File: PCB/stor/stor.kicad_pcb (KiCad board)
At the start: 2 copper layers, 21 x 55 mm, 45 parts, among them J1 Conn_01x04_Socket, SW1 TS1603-TZ38HBM, SW2 TS1603-TZ38HBM, U1 STM32H723VGT6, U2 TYPE-C 24P-GTJB 040, U3 USB3300-EZK-TR, U4 TPS62177DQCR, X1 25mhz, X2 32.768k, X3 24mhz

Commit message: all placed
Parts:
- moved C7 66.0 mm to (113.3, 50.0)
- moved C26 62.2 mm to (115.8, 68.7), turned to 90 degrees
- moved C17 60.5 mm to (121.3, 48.2)
- moved C10 56.8 mm to (114.5, 68.6), turned to 90 degrees
- moved C8 55.3 mm to (113.6, 64.8)
- moved C3 53.8 mm to (115.1, 66.8)
- moved C6 52.6 mm to (128.8, 50.1), turned to -90 degrees
- moved C4 48.1 mm to (121.0, 68.9), turned to 90 degrees
- moved C9 43.7 mm to (128.2, 65.3), turned to 90 degrees
- moved C5 42.2 mm to (129.5, 65.2), turned to 90 degrees
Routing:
- added copper zone on F.Cu, net GND

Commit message: pours
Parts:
- moved R4 2.70 mm to (129.1, 43.2)
- moved C16 2.41 mm to (126.7, 44.8)
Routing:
- added copper zone on In2.Cu, net /VDD
- added copper zone on B.Cu, net GND
- added copper zone on In1.Cu, net GND
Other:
- board size 21 x 55 mm -> 21 x 55.7 mm
- copper layers 2 -> 4
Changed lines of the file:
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@@
 	(layers
 		(0 "F.Cu" signal)
+		(4 "In1.Cu" signal)
+		(6 "In2.Cu" signal)
 		(2 "B.Cu" signal)
 		(9 "F.Adhes" user "F.Adhesive")
@@
 	)
 	(setup
+		(stackup
+			(layer "F.SilkS"
+				(type "Top Silk Screen")
+			)
+			(layer "F.Paste"
+				(type "Top Solder Paste")
+			)
+			(layer "F.Mask"
+				(type "Top Solder Mask")
+				(thickness 0.01)
+			)
+			(layer "F.Cu"
+				(type "copper")
+				(thickness 0.035)
+			)
+			(layer "dielectric 1"
+				(type "prepreg")
+				(thickness 0.1)
+				(material "FR4")
+				(epsilon_r 4.5)
+				(loss_tangent 0.02)
+			)
+			(layer "In1.Cu"
+				(type "copper")
+				(thickness 0.035)
+			)
+			(layer "dielectric 2"
+				(type "core")
+				(thickness 1.24)
+				(material "FR4")
+				(epsilon_r 4.5)
+				(loss_tangent 0.02)
+			)
+			(layer "In2.Cu"
+				(type "copper")
+				(thickness 0.035)
+			)
+			(layer "dielectric 3"
+				(type "prepreg")
+				(thickness 0.1)
+				(material "FR4")
+				(epsilon_r 4.5)
+				(loss_tangent 0.02)
+			)
+			(layer "B.Cu"
+				(type "copper")
+				(thickness 0.035)
+			)
+			(layer "B.Mask"
+				(type "Bottom Solder Mask")
+				(thickness 0.01)
+			)
+			(layer "B.Paste"
+				(type "Bottom Solder Paste")
+			)
+			(layer "B.SilkS"
+				(type "Bottom Silk Screen")
+			)
+			(copper_finish "None")
+			(dielectric_constraints no)
+		)
 		(pad_to_mask_clearance 0)
 		(allow_soldermask_bridges_in_footprints no)
@@
 		(capping no)
 		(filling no)
+		(zone_defaults)
 		(pcbplotparams
 			(layerselection 0x00000000_00000000_55555555_5755f5ff)
@@
 	(footprint "easyeda2kicad:R0402"
 		(layer "F.Cu")
-		(at 126.82 44.75)
+		(at 129.07 43.25)
 		(descr "200KΩ (2003) ±1%")
 		(property "Reference" "R4"
@@
 				(font
 					(size 1.27 1.27)
+					(thickness 0.15)
 				)
 			)
@@
 				(font
 					(size 1.27 1.27)
+					(thickness 0.15)
 				)
 			)
@@
 				(font
 					(size 1.27 1.27)
+					(thickness 0.15)
 				)
 			)
@@
 				(font
 					(size 1.27 1.27)
+					(thickness 0.15)
 				)
 			)
@@
 				(font
 					(size 1.27 1.27)
+					(thickness 0.15)
 				)
 			)
@@
 				(font
 					(size 1.27 1.27)
+					(thickness 0.15)
 				)
 			)
@@
 				(font
 					(size 1.27 1.27)
+					(thickness 0.15)
 				)
 			)
@@
 				(font
 					(size 1.27 1.27)
+					(thickness 0.15)
 				)
 			)
@@
 				(font
 					(size 1.27 1.27)
+					(thickness 0.15)
 				)
 			)
@@
 				(font
 					(size 1.27 1.27)
+					(thickness 0.15)
 				)
 			)
@@
 				(font
 					(size 1.27 1.27)
+					(thickness 0.15)
 				)
 			)
@@
 				(font
 					(size 1.27 1.27)
+					(thickness 0.15)
 				)
 			)
@@
 				(font
 					(size 1.27 1.27)
+					(thickness 0.15)
 				)
 			)
@@
 				(font
 					(size 1.27 1.27)
+					(thickness 0.15)
 				)
 			)
@@
 				(font
 					(size 1.27 1.27)
+					(thickness 0.15)
 				)
 			)
@@
 				(font
 					(size 1.27 1.27)
+					(thickness 0.15)
 				)
 			)
@@
 	(footprint "easyeda2kicad:C0402"
 		(layer "F.Cu")
-		(at 129.08 44.75)
+		(at 126.67 44.75)
 		(property "Reference" "C16"
 			(at 0 -4 0)
@@
 				(font
 					(size 1.27 1.27)
+					(thickness 0.15)
 				)
 			)
@@
 				(font
 					(size 1.27 1.27)
+					(thickness 0.15)
 				)
 			)
@@
 				(font
 					(size 1.27 1.27)
+					(thickness 0.15)
 				)
 			)
@@
 				(font
 					(size 1.27 1.27)
+					(thickness 0.15)
 				)
 			)
@@
 				(font
 					(size 1.27 1.27)
+					(thickness 0.15)
 				)
 			)
@@
 				(font
 					(size 1.27 1.27)
+					(thickness 0.15)
 				)
 			)
@@
 				(font
 					(size 1.27 1.27)
+					(thickness 0.15)
 				)
 			)
@@
 				(font
 					(size 1.27 1.27)
+					(thickness 0.15)
 				)
 			)
@@
 				(font
 					(size 1.27 1.27)
+					(thickness 0.15)
 				)
 			)
@@
 				(font
 					(size 1.27 1.27)
+					(thickness 0.15)
 				)
 			)
@@
 				(font
 					(size 1.27 1.27)
+					(thickness 0.15)
 				)
 			)
@@
 				(font
 					(size 1.27 1.27)
+					(thickness 0.15)
 				)
 			)
@@
 				(font
 					(size 1.27 1.27)
+					(thickness 0.15)
 				)
 			)
@@
 				(font
 					(size 1.27 1.27)
+					(thickness 0.15)
 				)
 			)
@@
 				(font
 					(size 1.27 1.27)
+					(thickness 0.15)
 				)
 			)
@@
 				(font
 					(size 1.27 1.27)
+					(thickness 0.15)
 				)
 			)
@@
 				(font
 					(size 1.27 1.27)
+					(thickness 0.15)
 				)
 			)
@@
 				(font
 					(size 1.27 1.27)
+					(thickness 0.15)
 				)
 			)
@@
 				(font
 					(size 1.27 1.27)
+					(thickness 0.15)
 				)
 			)
@@
 				(font
 					(size 1.27 1.27)
+					(thickness 0.15)
 				)
 			)
@@
 				(font
 					(size 1.27 1.27)
+					(thickness 0.15)
 				)
 			)
@@
 				(font
 					(size 1.27 1.27)
+					(thickness 0.15)
 				)
 			)
@@
 				(font
 					(size 1.27 1.27)
+					(thickness 0.15)
 				)
 			)
@@
 				(font
 					(size 1.27 1.27)
+					(thickness 0.15)
 				)
 			)
@@
 				(font
 					(size 1.27 1.27)
+					(thickness 0.15)
 				)
 			)
@@
 				(font
 					(size 1.27 1.27)
+					(thickness 0.15)
 				)
 			)
@@
 				(font
 					(size 1.27 1.27)
+					(thickness 0.15)
 				)
 			)
@@
 				(font
 					(size 1.27 1.27)
+					(thickness 0.15)
 				)
 			)
@@
 	)
 	(gr_rect
-		(start 110.5 39.75)
+		(start 110.5 39.05)
 		(end 131.5 94.75)
 		(radius 3)
@@
 	(zone
 		(net "GND")
-		(layer "F.Cu")
+		(layers "F.Cu" "B.Cu")
 		(hatch edge 0.5)
 		(connect_pads
@@
 			)
 		)
+	)
+	(zone
+		(net "GND")
+		(layer "In1.Cu")
+		(hatch edge 0.5)
+		(connect_pads
+			(clearance 0.5)
+		)
+		(min_thickness 0.25)
+		(fill yes
+			(thermal_gap 0.5)
+			(thermal_bridge_width 0.5)
+			(island_removal_mode 0)
+		)
+		(polygon
+			(pts
+				(xy 106.5 30) (xy 136.5 30) (xy 136.5 100) (xy 106.5 100)
+			)
+		)
+	)
+	(zone
+		(net "/VDD")
+		(layer "In2.Cu")
+		(hatch edge 0.5)
+		(connect_pads
+			(clearance 0.5)
+		)
+		(min_thickness 0.25)
+		(fill yes
+			(thermal_gap 0.5)
+			(thermal_bridge_width 0.5)
+			(island_removal_mode 0)
+		)
+		(polygon
+			(pts
+				(xy 107.5 30) (xy 137.5 30) (xy 137.5 100) (xy 107.5 100)
+			)
+		)

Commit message: some routing
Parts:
- moved C10 13.7 mm to (128.1, 67.3)
- moved R2 13.6 mm to (129.1, 41.1), turned to 180 degrees
- moved C13 0.35 mm to (117.3, 66.8)
- moved C12 0.33 mm to (121.0, 67.2)
- moved C14 0.31 mm to (119.1, 66.6)
- moved C24 0.30 mm to (115.0, 43.4)
- moved X2 0.25 mm to (118.3, 68.5)
- moved X1 0.15 mm to (125.1, 68.0)
- moved C4 0.10 mm to (121.0, 69.0)
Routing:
- net /VDD: track 0.00 -> 23.0 mm, vias 0 -> 14
- net /XI: track 0.00 -> 14.0 mm
- net Net-(C20-Pad2): track 0.00 -> 8.46 mm
- net /XO: track 0.00 -> 7.28 mm
- net /PH1: track 0.00 -> 6.78 mm
- net /PH0: track 0.00 -> 6.18 mm
- net GND: track 0.00 -> 6.10 mm, vias 0 -> 16
- net /VCAP1: track 0.00 -> 1.47 mm
- net Net-(C18-Pad2): track 0.00 -> 1.06 mm

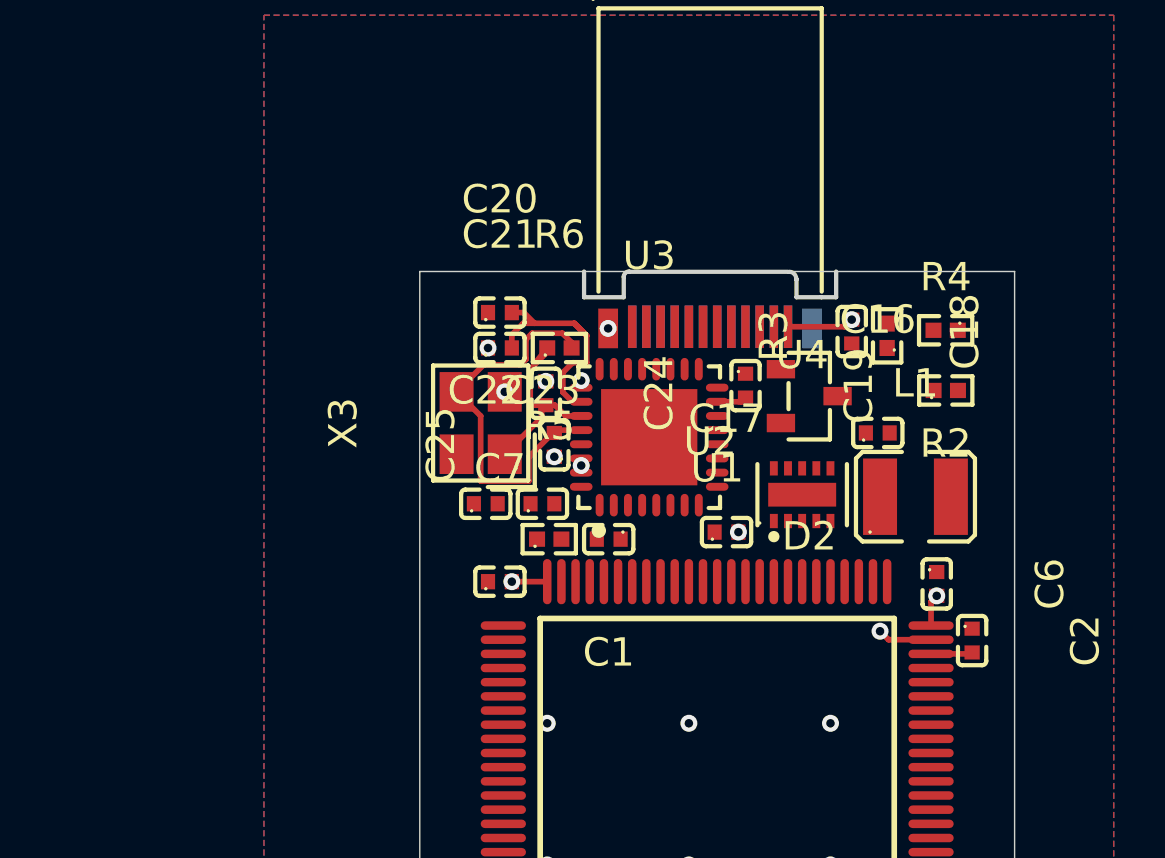
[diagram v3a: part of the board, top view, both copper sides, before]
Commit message: crazy refactor to accomodate diffpair
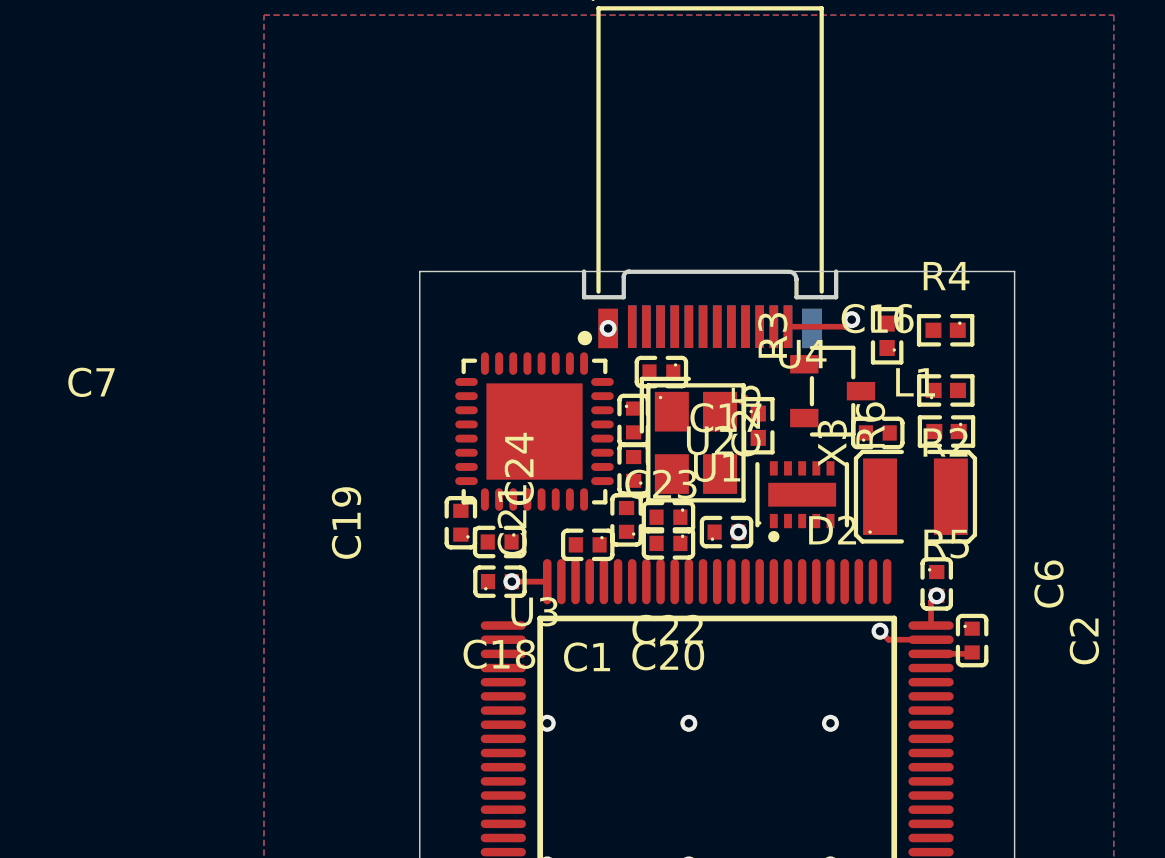
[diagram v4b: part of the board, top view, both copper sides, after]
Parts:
- moved R5 14.5 mm to (129.1, 44.7), turned to 180 degrees
- moved C18 14.5 mm to (113.3, 48.6), turned to 180 degrees
- moved C19 11.2 mm to (112.0, 47.9), turned to 90 degrees
- moved C20 10.1 mm to (119.3, 48.6), turned to 180 degrees
- moved X3 7.63 mm to (120.2, 45.1), turned to -90 degrees
- moved C21 7.54 mm to (117.8, 47.8), turned to 90 degrees
- moved R6 7.54 mm to (122.5, 44.5), turned to -90 degrees
- moved C22 6.47 mm to (119.3, 47.7), turned to 180 degrees
- moved C23 6.27 mm to (119.0, 42.6), turned to 180 degrees
- moved C24 4.09 mm to (118.0, 46.0), turned to 90 degrees
- moved U3 4.05 mm to (114.5, 44.7), turned to 180 degrees
- moved C25 2.93 mm to (118.0, 44.3), turned to -90 degrees
- moved D2 0.84 mm to (125.1, 43.3)
- moved C1 0.77 mm to (116.4, 48.7)
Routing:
- net /XI: track 14.0 -> 0.00 mm
- net Net-(C20-Pad2): track 8.46 -> 0.00 mm
- net /XO: track 7.28 -> 0.00 mm
- net Net-(C18-Pad2): track 1.06 -> 0.21 mm
- net GND: vias 16 -> 12
- net /VDD: vias 14 -> 12

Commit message: soo much routing
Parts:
- added R10: 10k, easyeda2kicad:R0402, F.Cu at (125.3, 79.3)
- added R11: 10k, easyeda2kicad:R0402, F.Cu at (122.5, 76.1)
- added R7: 10k, easyeda2kicad:R0402, F.Cu at (120.9, 78.0)
- added R8: 10k, easyeda2kicad:R0402, F.Cu at (112.1, 80.0)
- added R9: 10k, easyeda2kicad:R0402, F.Cu at (120.9, 77.0)
- moved R5 5.27 mm to (130.2, 49.8), turned to 90 degrees
- moved D2 0.87 mm to (124.4, 43.8)
- moved C8 0.68 mm to (112.9, 64.8), turned to 90 degrees
- moved U2 0.50 mm to (120.2, 41.0)
- turned R6 to 90 degrees
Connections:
- U1 pad 80: unconnected-(U1-PC12-Pad80) -> /PC12
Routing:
- net /PC12: track 0.00 -> 61.2 mm
- net /PC11: track 0.00 -> 43.6 mm, vias 0 -> 2
- net /PC10: track 0.00 -> 43.1 mm, vias 0 -> 2
- net /PC8: track 0.00 -> 43.0 mm, vias 0 -> 2
- net /PC9: track 0.00 -> 40.5 mm, vias 0 -> 2
- net /PA5: track 0.00 -> 38.0 mm, vias 0 -> 2
- net /SWCLK: track 0.00 -> 32.9 mm, vias 0 -> 1
- net /PD2: track 0.00 -> 31.8 mm, vias 0 -> 2
- net /PC3: track 0.00 -> 31.2 mm, vias 0 -> 2
- net /PC0: track 0.00 -> 31.1 mm, vias 0 -> 2
- net /PC2: track 0.00 -> 31.0 mm, vias 0 -> 2
- net /PD4: track 0.00 -> 25.5 mm
- net /SWDIO: track 0.00 -> 24.1 mm, vias 0 -> 1
- net /PA3: track 0.00 -> 22.5 mm, vias 0 -> 2
- net /PB1: track 0.00 -> 21.8 mm, vias 0 -> 2
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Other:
- board size 21 x 55.7 mm -> 22 x 55.7 mm

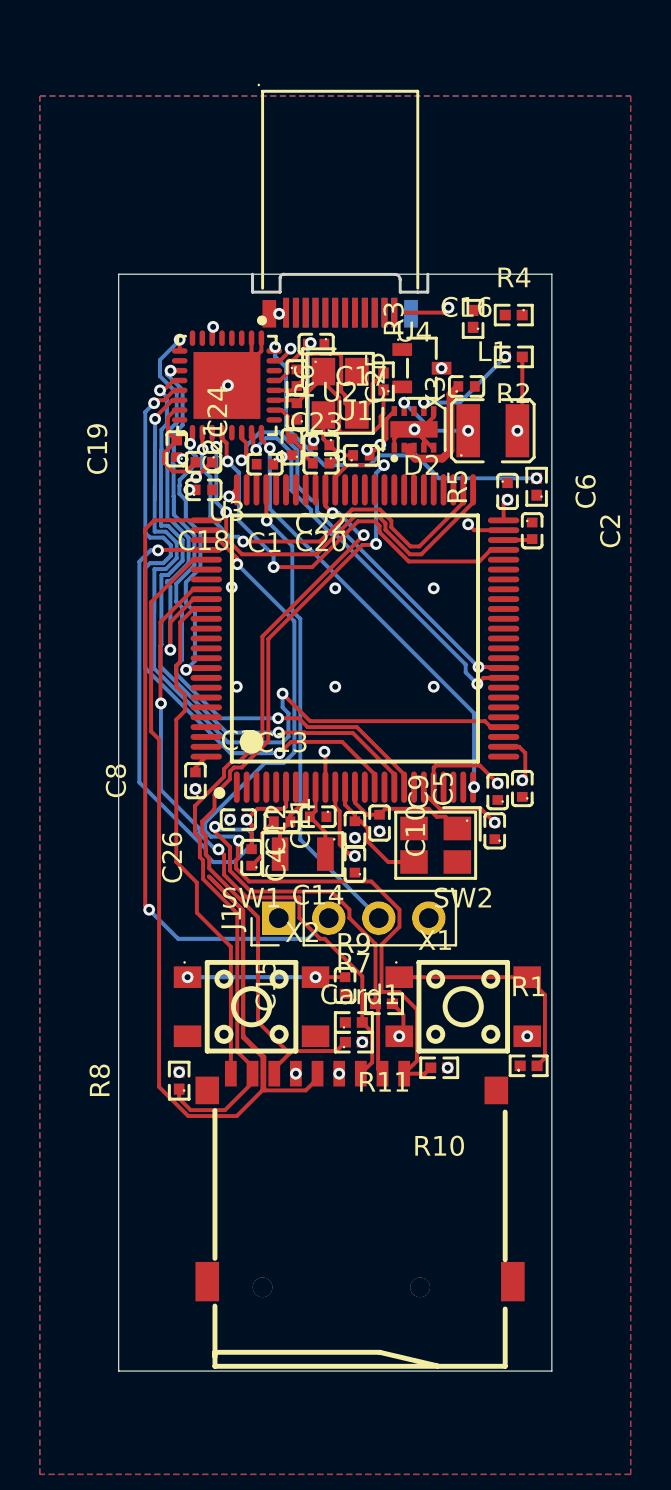
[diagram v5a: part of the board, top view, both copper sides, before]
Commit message: new usb and uh finish routing!
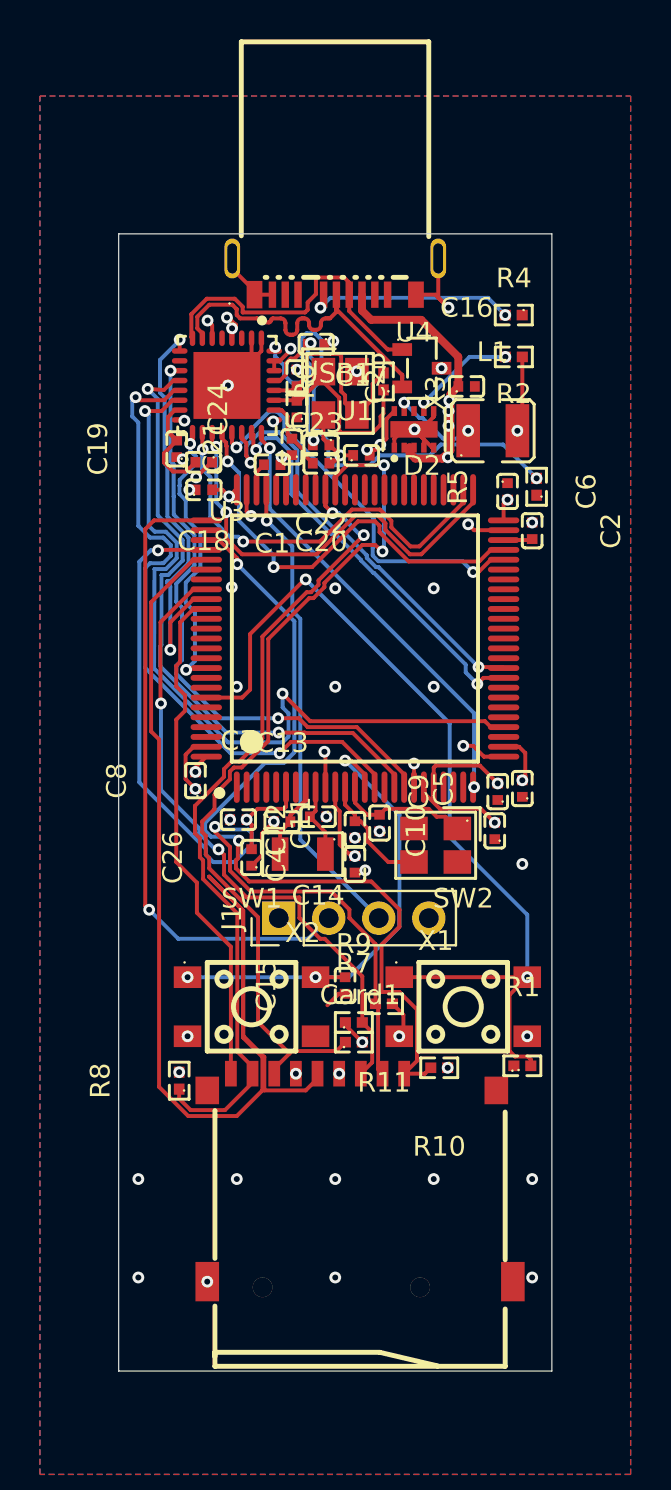
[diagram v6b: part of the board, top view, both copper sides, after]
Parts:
- removed R3: 5.1k, easyeda2kicad:R0402
- removed U2: TYPE-C 24P-GTJB 040, easyeda2kicad:USB-C-SMD_TYPE-C-24P-GTJB-040
- added USB1: GT-USB-8016A, easyeda2kicad:USB-TYPE-C-SMD_GT-USB-8016A, F.Cu at (120.0, 39.2)
- moved C1 0.37 mm to (116.8, 48.7)
- moved R1 0.32 mm to (129.5, 79.2)
- moved C24 0.12 mm to (118.0, 45.9)
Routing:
- net /BOOT0: track 11.5 -> 46.3 mm, vias 0 -> 2
- net /VBUS: track 6.08 -> 35.5 mm, vias 0 -> 6
- net /PB10: track 0.00 -> 19.7 mm, vias 0 -> 2
- net /D+: track 0.00 -> 18.1 mm
- net /D-: track 0.00 -> 16.5 mm
- net /NRST: track 8.00 -> 24.2 mm, vias 2 -> 3
- net GND: track 23.9 -> 38.2 mm, vias 23 -> 43
- net /CC1: track 0.00 -> 10.2 mm, vias 0 -> 2
- net Net-(U3-RBIAS): track 18.7 -> 25.3 mm
- net /VDD: track 32.3 -> 35.5 mm, vias 18 -> 21
- net /VCAP2: track 0.00 -> 1.43 mm
- net /PC0: track 31.1 -> 32.5 mm
- net /PA5: track 38.0 -> 39.0 mm
- net /PC8: track 43.0 -> 43.8 mm
- net /PC3: track 31.2 -> 30.7 mm
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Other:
- board size 22 x 55.7 mm -> 22 x 57.8 mm

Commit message: smal changes
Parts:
- moved R2 5.89 mm to (124.1, 44.3)
- moved D2 2.54 mm to (122.5, 42.2), turned to 90 degrees
- moved USB1 1.00 mm to (120.0, 38.2)
- moved C24 0.36 mm to (118.1, 46.3)
- moved R5 0.32 mm to (129.9, 49.8)
- moved R6 0.30 mm to (122.5, 44.8)
- moved C25 0.27 mm to (118.1, 44.6)
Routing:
- net /PC12: track 61.2 -> 37.2 mm
- net GND: track 38.2 -> 59.4 mm, vias 43 -> 63
- net Net-(U3-RBIAS): track 25.3 -> 17.4 mm
- net /PC11: track 43.6 -> 38.5 mm
- net /D+: track 18.1 -> 14.6 mm
- net /CC1: track 10.2 -> 6.97 mm
- net /D-: track 16.5 -> 17.9 mm
- net /PC10: track 43.1 -> 41.8 mm
- net /PB12: track 21.5 -> 20.3 mm
- net /PB13: track 20.4 -> 19.3 mm
- net /VBUS: track 35.5 -> 34.7 mm, vias 6 -> 5
- net /VDD: track 35.5 -> 35.2 mm, vias 21 -> 20
- net /BOOT0: vias 2 -> 3
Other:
- board size 22 x 57.8 mm -> 22 x 58.8 mm

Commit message: fussed with the routing I guess
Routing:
- net /PA5: track 39.0 -> 37.2 mm
- net /PC0: track 32.5 -> 30.9 mm
- net /PC3: track 30.7 -> 31.5 mm
- net /PC11: track 38.5 -> 37.8 mm
- net /PB13: track 19.3 -> 18.7 mm
- net /PB12: track 20.3 -> 19.6 mm
- net /SWCLK: track 32.9 -> 32.2 mm
- net GND: track 59.4 -> 59.1 mm, vias 63 -> 62
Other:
- outline, holes or cut-outs redrawn
